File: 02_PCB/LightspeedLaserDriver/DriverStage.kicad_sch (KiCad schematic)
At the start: 14 parts, among them Q1 FMMT417TD

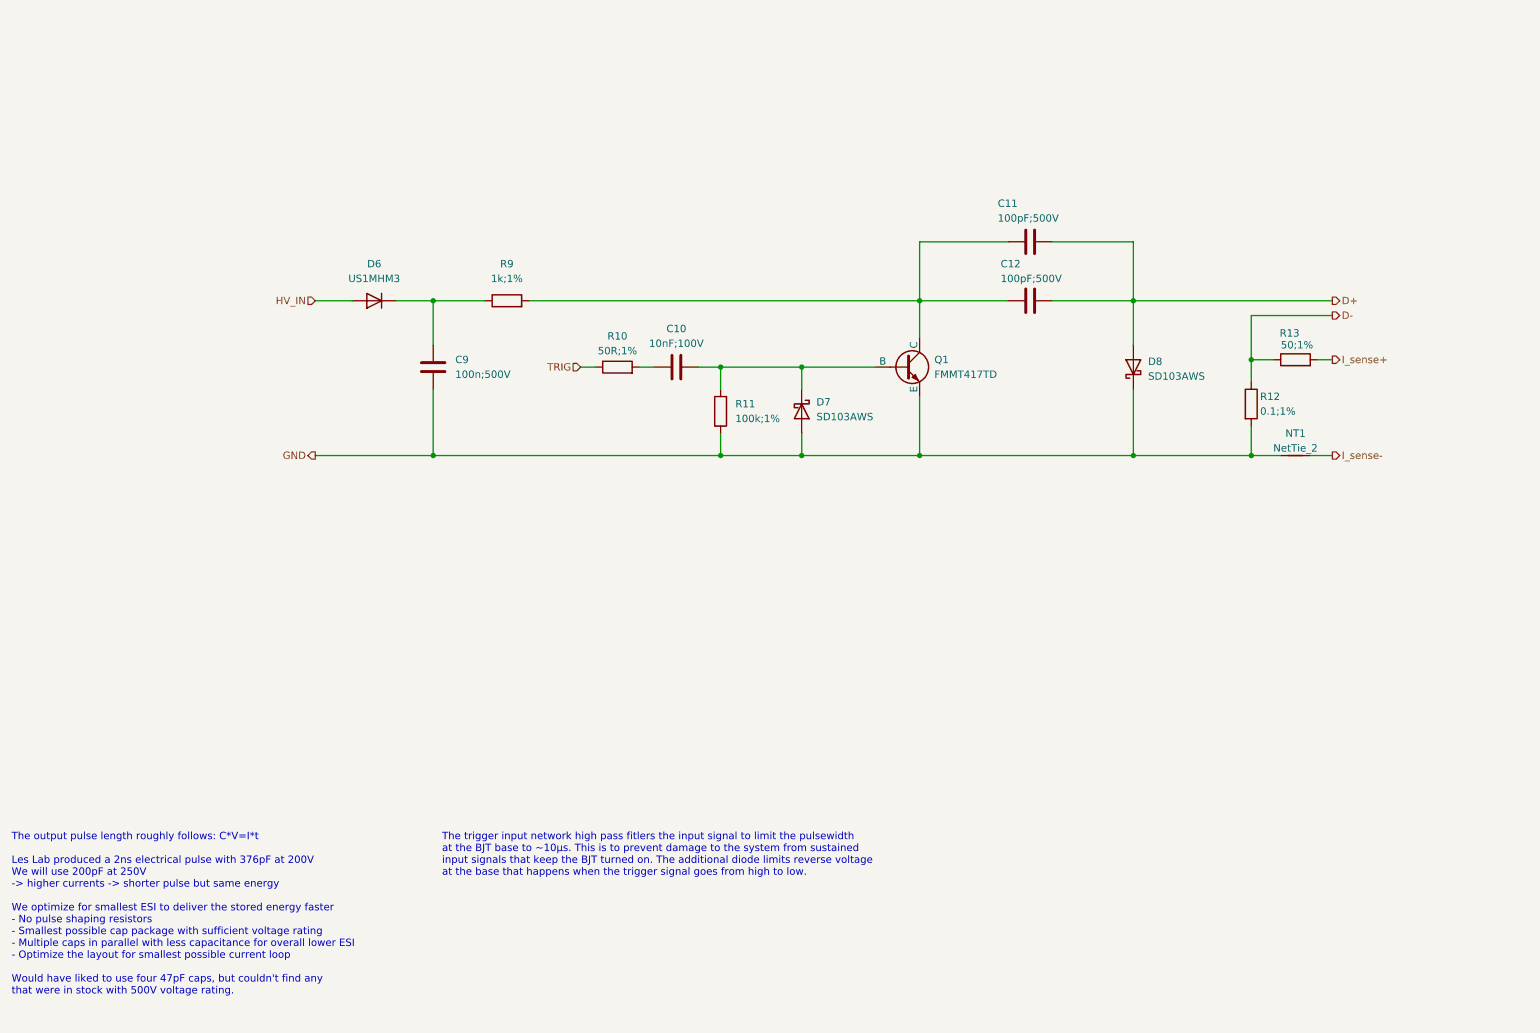
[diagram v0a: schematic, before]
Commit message: feat(pcb): route all traces
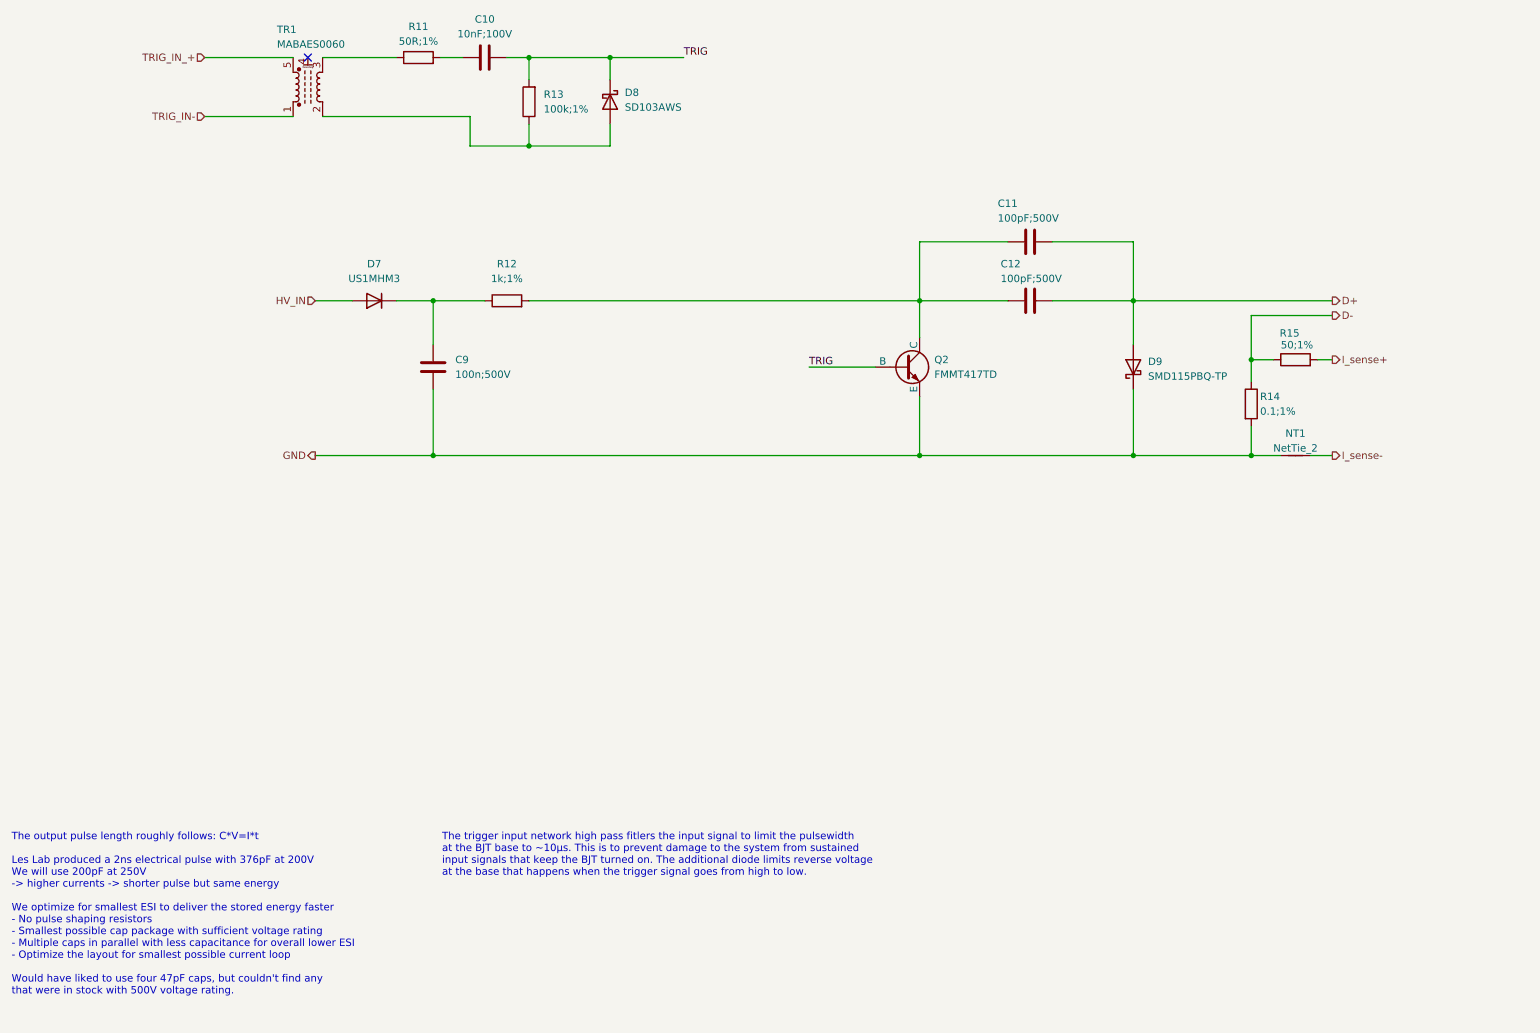
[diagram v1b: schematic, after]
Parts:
- added TR1: MABAES0060, Transformer_SMD:Transformer_MACOM_SM-22, symbol Transformer:ETC1-1-13
- D9: renamed from D8; value SD103AWS -> SMD115PBQ-TP; footprint Diode_SMD:D_SOD-323 -> CustomFootprints:D_SOD-323HE
- renumbered D6 to D7, D7 to D8, Q1 to Q2, R10 to R11, R9 to R12, R11 to R13, R12 to R14, R13 to R15
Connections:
- net GND: no longer D8.2 (A), R13.1
- net TRIG: now also C10.2, D8.1 (K), Q2.2 (B), R13.2; no longer R11.1
- new net: D8.2 (A), R13.1, TR1.2
- new net: R11.1, TR1.3
- new net TRIG_IN-: TR1.1
- new net TRIG_IN_+: TR1.5
- no-connect marks 0 -> 1
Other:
- moved on the sheet: C10, D8, R11, R13

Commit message: feat(pcb): laser driver layout draft finished, add high voltage indicator LED and discharge path
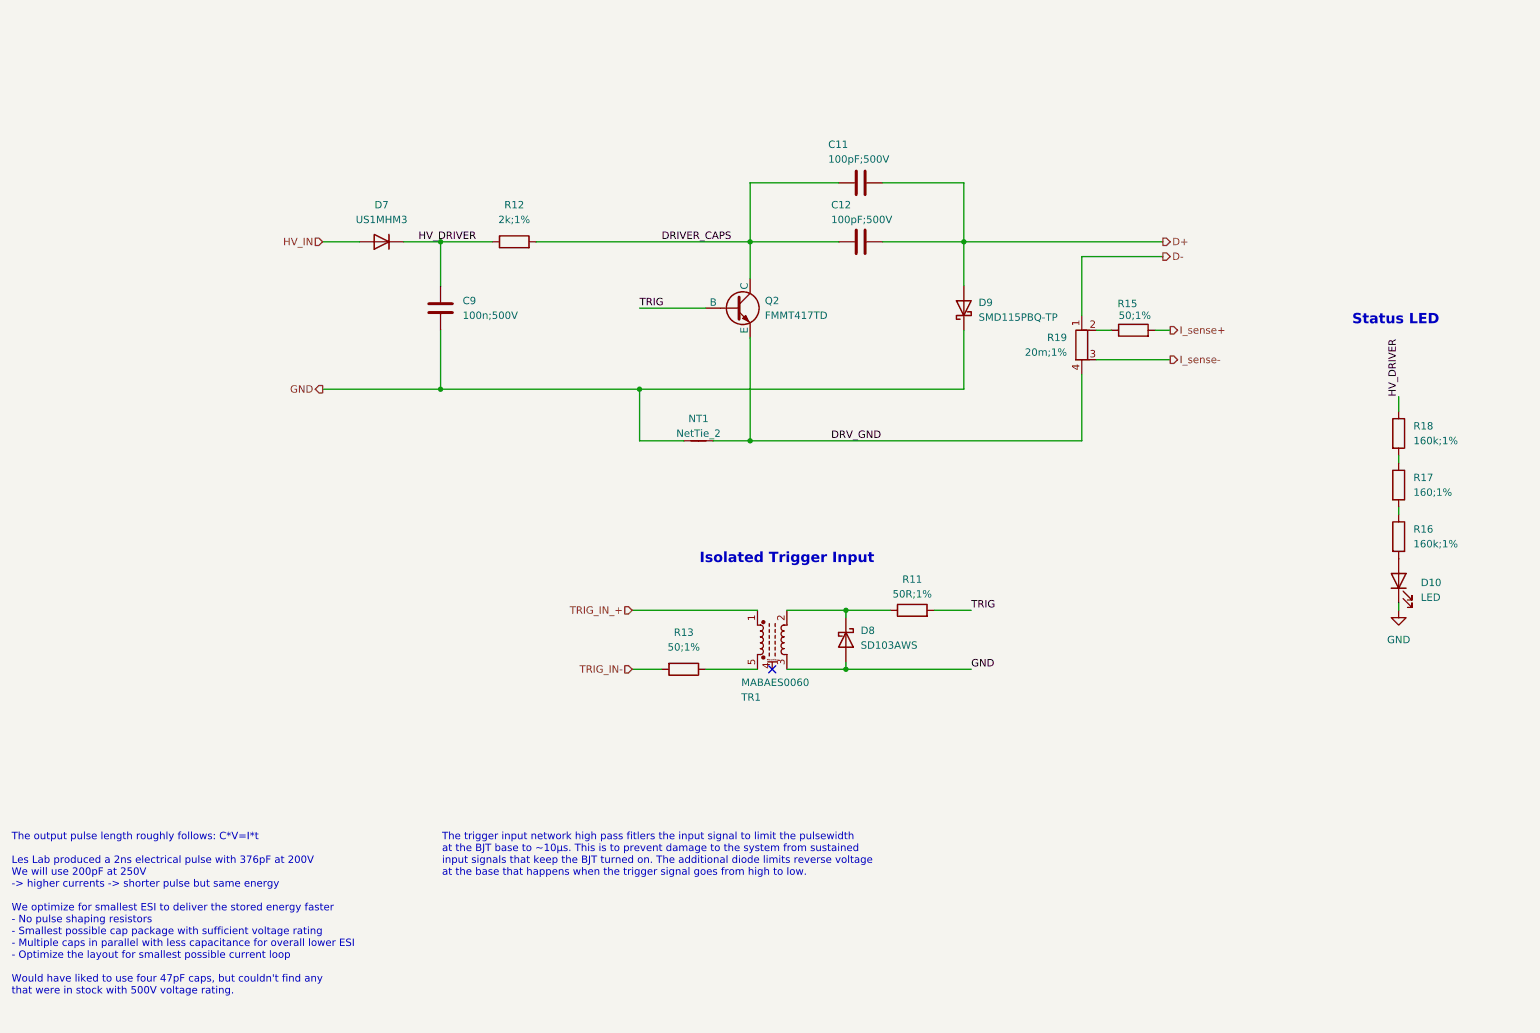
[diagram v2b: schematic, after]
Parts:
- removed C10: 10nF;100V, Capacitor_SMD:C_0603_1608Metric, symbol Device:C
- removed R14: 0.1;1%, Resistor_SMD:R_0603_1608Metric, symbol Device:R
- added D10: LED, LED_SMD:LED_0603_1608Metric, symbol Device:LED
- added R16, R18: 160k;1%, Resistor_SMD:R_0603_1608Metric, symbol Device:R
- added R17: 160;1%, Resistor_SMD:R_0603_1608Metric, symbol Device:R
- added R19: 20m;1%, CustomFootprints:FC4L16, symbol Device:R_Shunt
- R12: value 1k;1% -> 2k;1%
- R13: value 100k;1% -> 50;1%
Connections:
- net D-: now also R19.1; no longer R15.1
- net GND: now also D8.2 (A), TR1.3, D10.1 (K); no longer Q2.3 (E)
- net I_sense-: now also R19.3; no longer NT1.2
- net TRIG: now also R11.2; no longer D8.1 (K), R13.2
- net TRIG_IN-: now also R13.2; no longer TR1.1
- net TRIG_IN_+: now also TR1.1; no longer TR1.5
- net HV_DRIVER: now reaches C9.1, D7.1 (K), R12.1
- net HV_DRIVER: now also R18.1
- net at R11.1: now also D8.1 (K), TR1.2; no longer TR1.3
- net DRIVER_CAPS: now reaches C11.1, C12.1, Q2.1 (C), R12.2
- new net: R17.1, R18.2
- new net: D10.2 (A), R16.2
- new net: R16.1, R17.2
- new net: R13.1, TR1.5
- new net: R15.1, R19.2
- new net DRV_GND: NT1.2, Q2.3 (E), R19.4
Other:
- note added: "Isolated Trigger Input"
- note added: "Status LED"
- moved on the sheet: C11, C12, C9, D7, D8, D9, NT1, Q2, R11, R12, R13, R15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

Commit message: feat(pcb): improve the design draft
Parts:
- added R14: 2k;1%, Resistor_SMD:R_0805_2012Metric, symbol Device:R
- added R20: 100k;1%, Resistor_SMD:R_0603_1608Metric, symbol Device:R
- C11, C12: value 100pF;500V -> 100p;500V
- D10: value LED -> APTD1608LSURCK
- R11: value 50R;1% -> 50;1%
- R17: value 160;1% -> 160k;1%
- R19: value 20m;1% -> FC4L16R020FER
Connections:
- net DRIVER_CAPS: now also Q2.3 (C); no longer Q2.1 (C)
- net DRV_GND: now also Q2.2 (E), R14.1; no longer Q2.3 (E)
- net GND: now also TR1.4 (MP), R20.2; no longer D9.1 (K)
- net TRIG: now also D8.1 (K), Q2.1 (B), R20.1; no longer Q2.2 (B)
- net at R11.1, TR1.2: no longer D8.1 (K)
- new net: D9.1 (K), R14.2
- no-connect marks 1 -> 0
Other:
- note added: "The trigger input uses a wideband RF transformwe to galvannically isolate the trigger input to protect the connected signal source. This also limits the trigger pulse width which prevents damage to the system from sustained input signals that keep the BJT turned on. The additional diode limits reverse voltage at the base that happens when the trigger signal goes from high to low."
- note removed: "The trigger input network high pass fitlers the input signal to limit the pulsewidth at the BJT base to ~10µs. This is to prevent damage to the system from sustained input signals that keep the BJT turned on. The additional diode limits reverse voltage at the base that happens when the trigger signal goes from high to low."
- moved on the sheet: D8, D9, NT1, R11, R12, R15
